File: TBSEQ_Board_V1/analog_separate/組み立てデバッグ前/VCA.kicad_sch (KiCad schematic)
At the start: 37 parts, among them IC15 CA3080A, J4 Conn_01x02_Pin, Q31 PNP, Q32 NPN

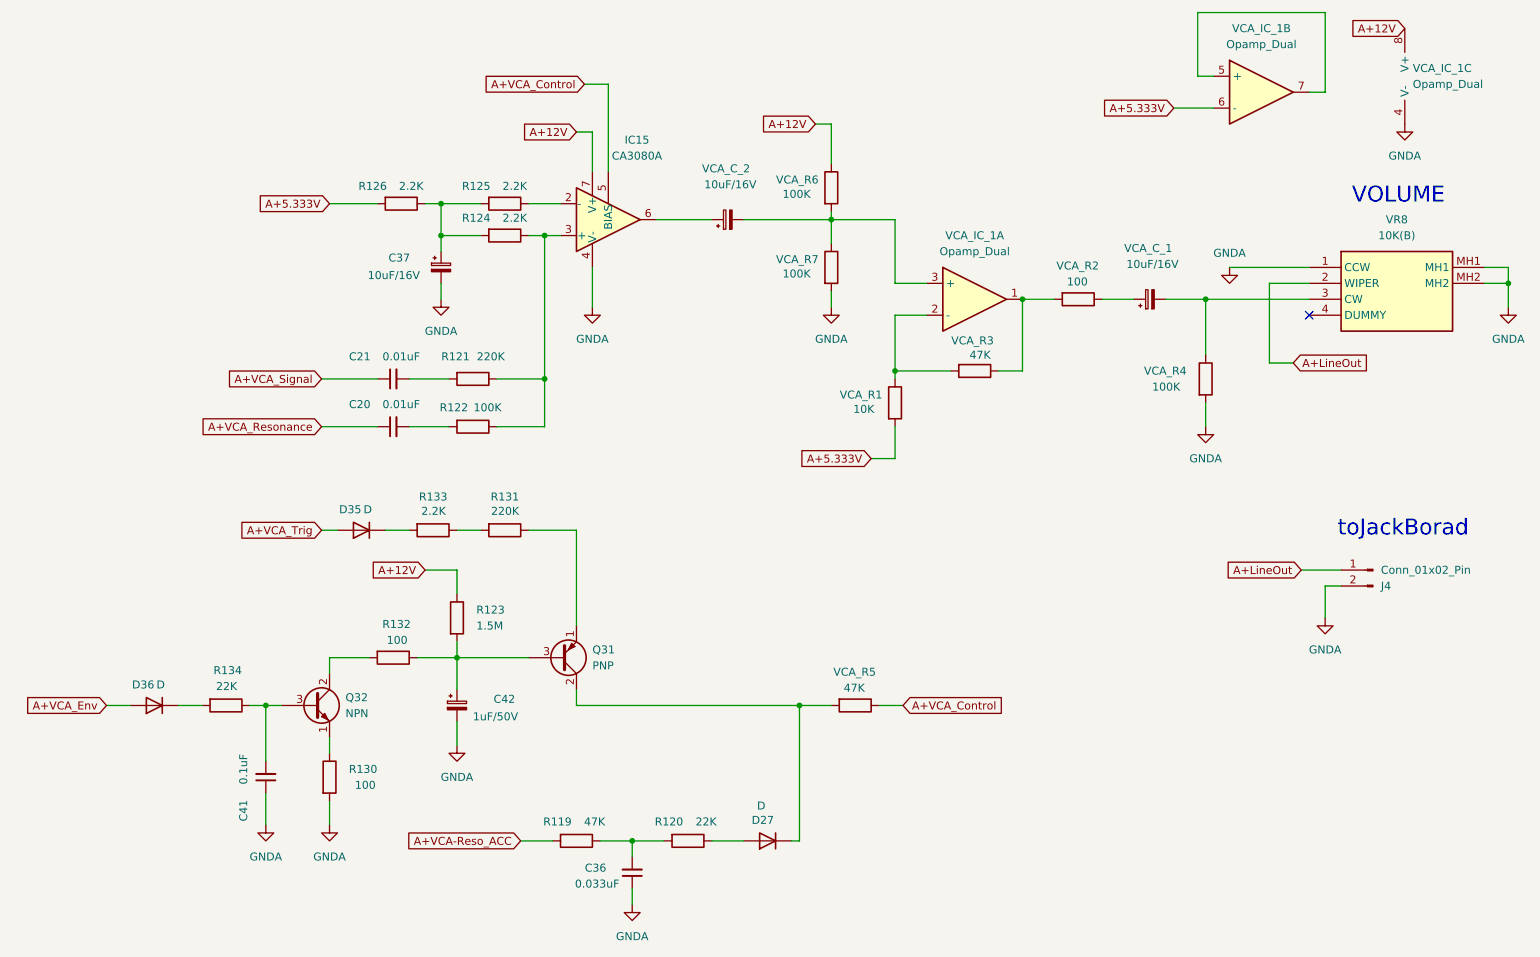
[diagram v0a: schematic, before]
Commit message: analog_separate fix
実装してバグを修正
・VR6以外のボリュームの左右が逆なのを修正
・デュアルトランジスタをHN1C01FU-GRに変更
・VCA CA3080後の出力段のバイアス/増幅率等の設計ミスを修正
・入力信号のシルク位置が間違っているので修正
⇒それ以外は正常動作を確認済
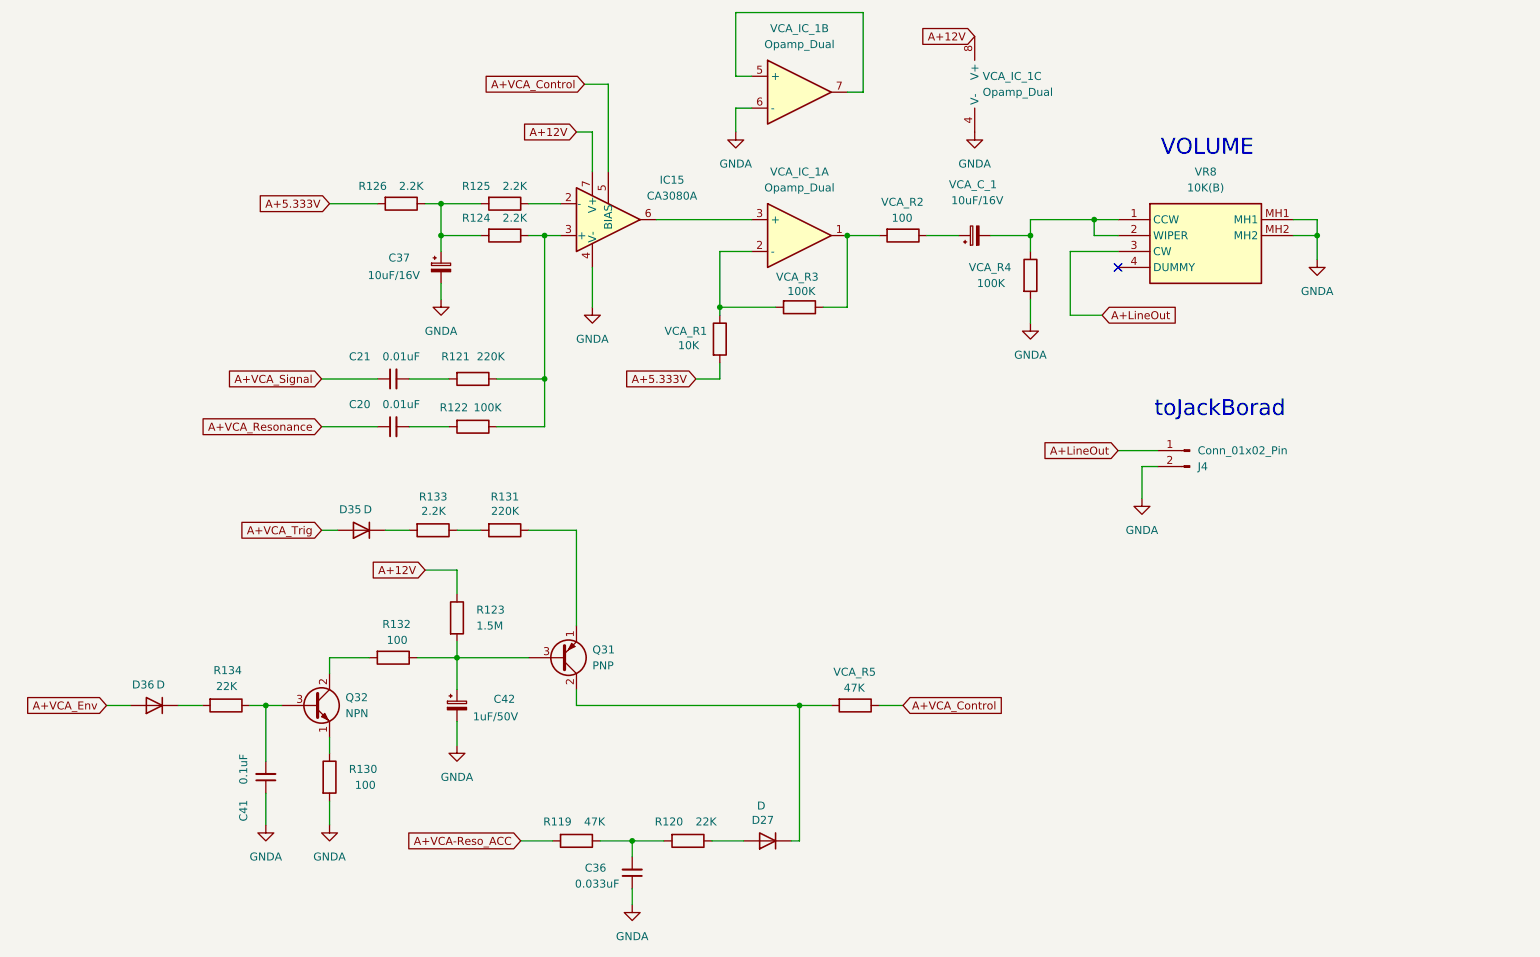
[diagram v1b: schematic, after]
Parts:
- removed VCA_C_2: 10uF/16V, Capacitor_THT:CP_Radial_D4.0mm_P2.00mm, symbol Device:C_Polarized_Small
- removed VCA_R6, VCA_R7: 100K, Resistor_THT:R_Axial_DIN0207_L6.3mm_D2.5mm_P2.54mm_Vertical, symbol Device:R
- VCA_R3: value 47K -> 100K
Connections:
- net A+5.333V: no longer VCA_IC_1.6 (-)
- net A+LineOut: now also VR8.3 (CW); no longer VR8.2 (WIPER)
- net GNDA: now also VCA_IC_1.6 (-); no longer VR8.1 (CCW)
- net at IC15.6: now also VCA_IC_1.3 (+)
- net at VCA_C_1.2, VCA_R4.1: now also VR8.1 (CCW), VR8.2 (WIPER); no longer VR8.3 (CW)
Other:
- moved on the sheet: J4, VCA_C_1, VCA_IC_1A, VCA_IC_1B, VCA_IC_1C, VCA_R1, VCA_R2, VCA_R3, VCA_R4, VR8
